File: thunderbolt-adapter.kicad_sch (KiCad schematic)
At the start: 95 parts, among them J1 DX07S024JJ2R1300, J2 PCIe_x4_Conn_EdgeMount, U1 SI52112-B6-GT, U2 AP62301WU-7, U3 TPS65983BAZBHR, U4 JHL6340SLLSQ, U5 MX25L8006EM1I-12G, Y1 25MHz

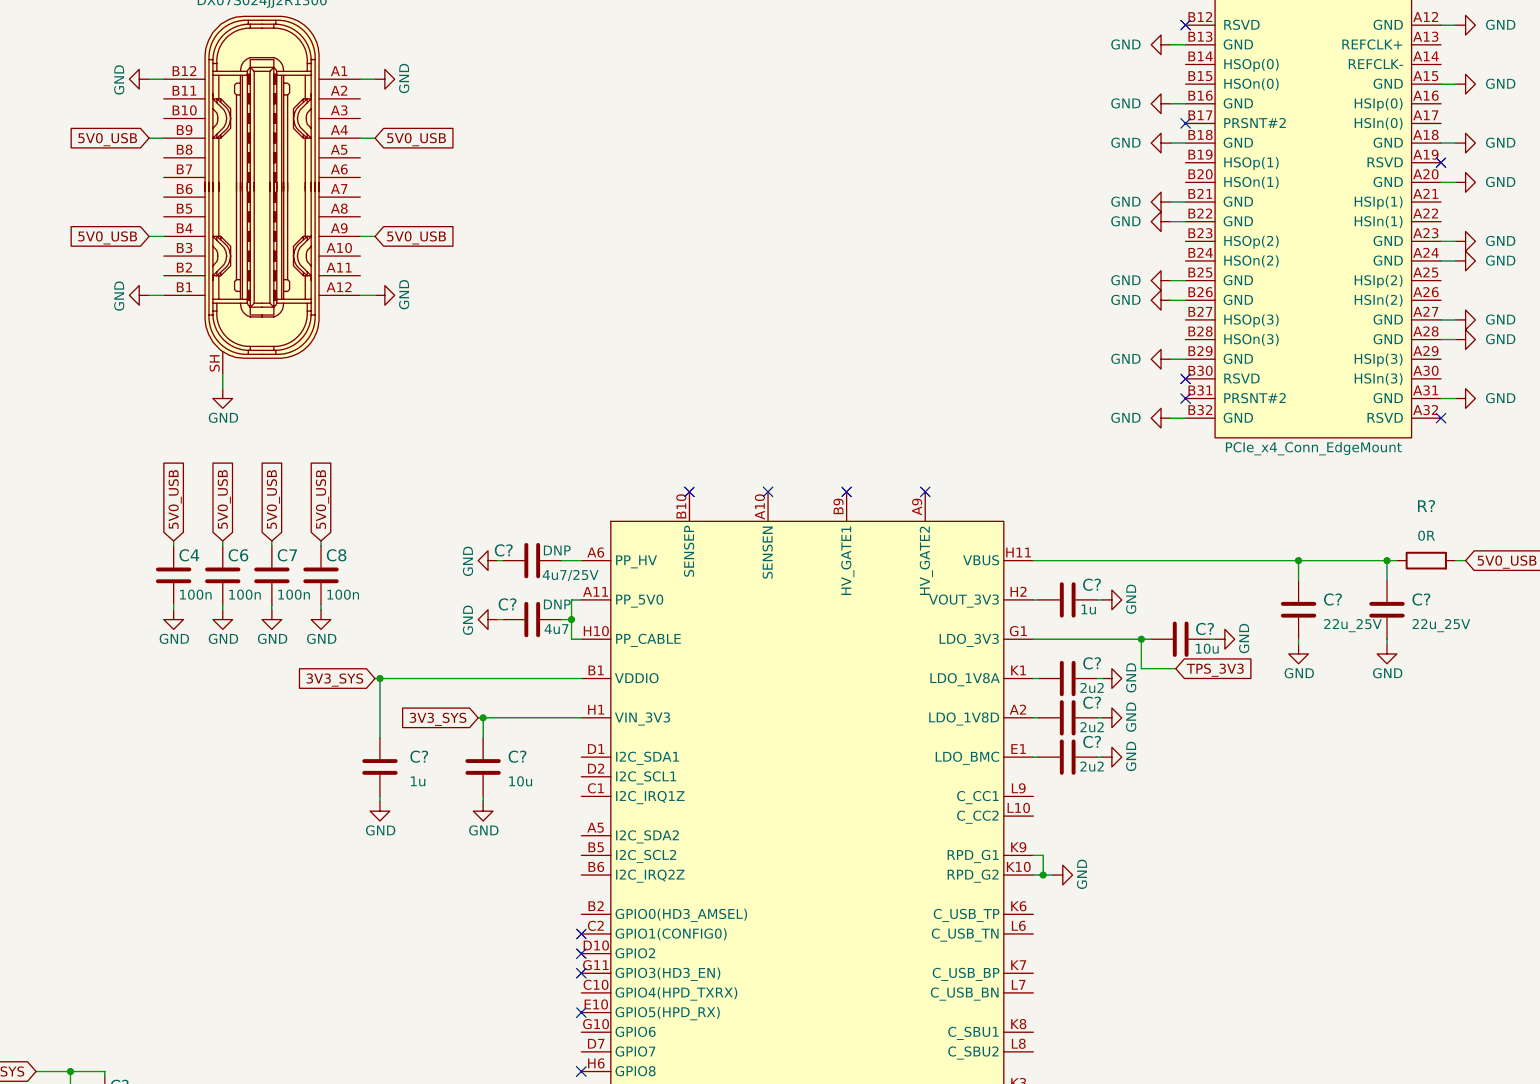
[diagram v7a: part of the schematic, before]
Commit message: Connect USB CC lanes
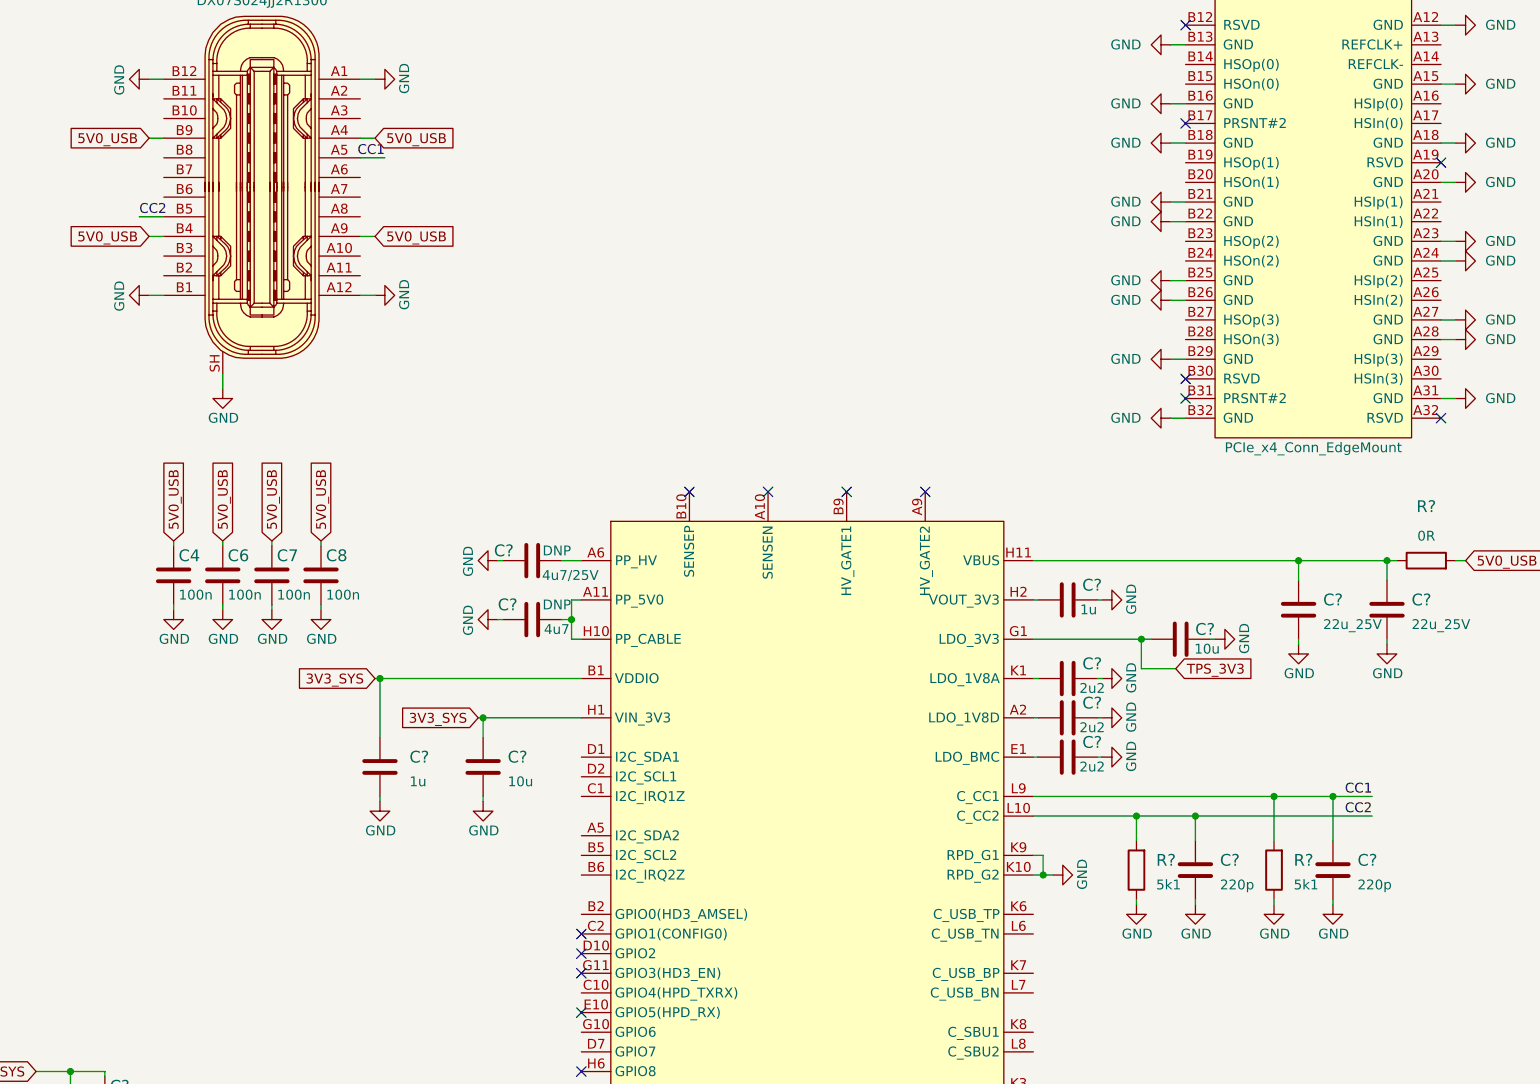
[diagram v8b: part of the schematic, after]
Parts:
- added C? (x2): C_220p_0402, antmicro-footprints:0402-cap, symbol antmicroCapacitors0402:C_220p_0402
- added R? (x2): R_5k1_0402, antmicro-footprints:0402-res, symbol antmicroResistors0402:R_5k1_0402
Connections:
- net GND: now also C?.2, C?.2, R?.1, R?.1
- net CC1: now reaches J1.A5
- net CC1: now also U3.L9 (C_CC1), C?.1, R?.2
- net CC2: now reaches J1.B5
- net CC2: now also U3.L10 (C_CC2), C?.1, R?.2
